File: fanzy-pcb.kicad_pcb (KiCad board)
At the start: 2 copper layers, 68 x 45 mm, 20 parts, among them J1 Conn_01x04_Pin, J2 Screw_Terminal_01x05, Q1 IRLZ44N, SW1 SW_Push, U1 STM32G030F6Px, U4 YAAJ_DCDC_StepDown_LM2596

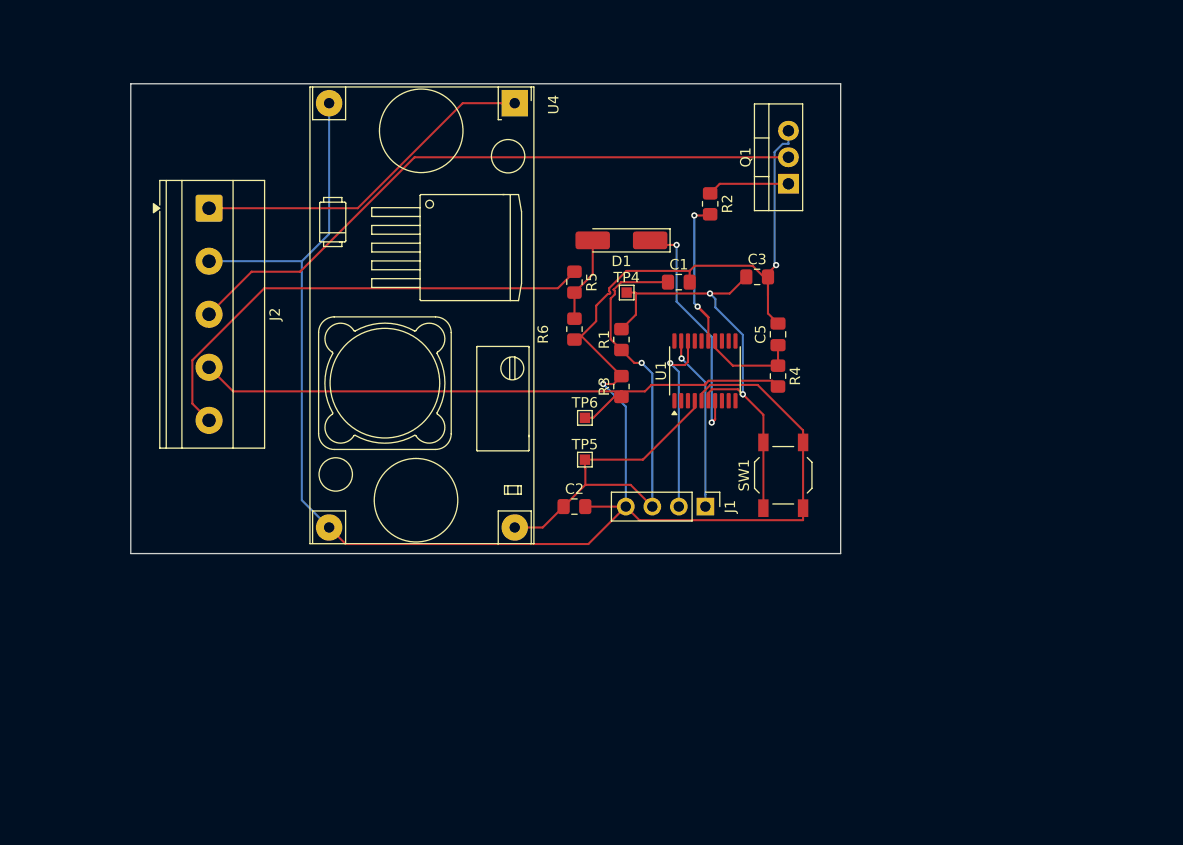
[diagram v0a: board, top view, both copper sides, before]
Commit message: feat: uart port + rework
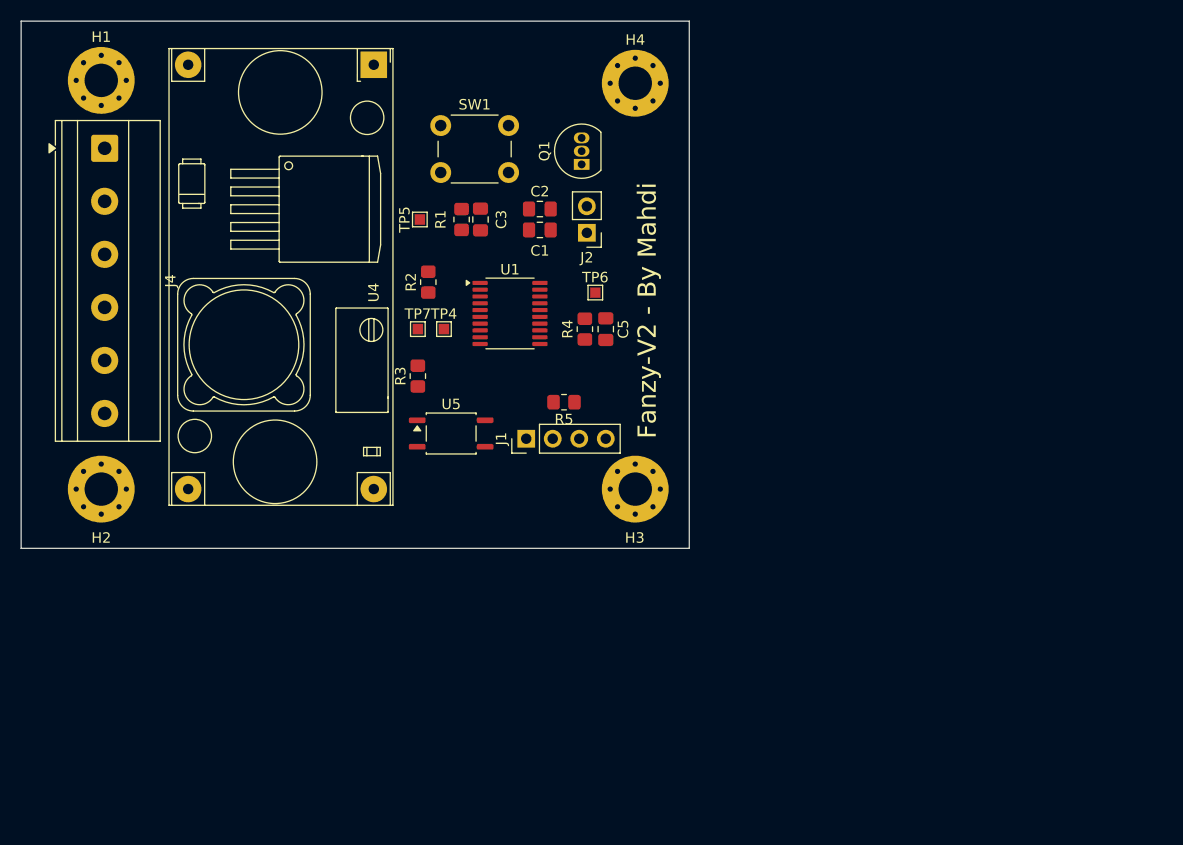
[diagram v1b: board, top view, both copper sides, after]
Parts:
- removed D1: 2V, Diode_SMD:D_MiniMELF_Handsoldering
- removed R6: 10k, Resistor_SMD:R_0805_2012Metric_Pad1.20x1.40mm_HandSolder
- added H1: MountingHole_Pad, MountingHole:MountingHole_3.2mm_M3_Pad_Via, F.Cu at (89.7, 51.2)
- added H2: MountingHole_Pad, MountingHole:MountingHole_3.2mm_M3_Pad_Via, F.Cu at (89.7, 90.3)
- added H3: MountingHole_Pad, MountingHole:MountingHole_3.2mm_M3_Pad_Via, F.Cu at (140.8, 90.3)
- added H4: MountingHole_Pad, MountingHole:MountingHole_3.2mm_M3_Pad_Via, F.Cu at (140.8, 51.5)
- added J4: Screw_Terminal_01x06, TerminalBlock_Phoenix:TerminalBlock_Phoenix_MKDS-1,5-6-5.08_1x06_P5.08mm_Horizontal, F.Cu at (90.0, 57.7)
- added TP7: TestPoint, TestPoint:TestPoint_Pad_1.0x1.0mm, F.Cu at (120.0, 75.0)
- added U5: TLP185, Octocoupler:TLP185, F.Cu at (123.2, 85.0)
- J2: value Screw_Terminal_01x05 -> Conn_01x02_Pin; footprint TerminalBlock_Phoenix:TerminalBlock_Phoenix_MKDS-1,5-5-5.08_1x05_P5.08mm_Horizontal -> Connector_PinHeader_2.54mm:PinHeader_1x02_P2.54mm_Vertical
- Q1: value IRLZ44N -> PN2222A; footprint Package_TO_SOT_THT:TO-220-3_Vertical -> Package_TO_SOT_THT:TO-92_Inline
- R5: value 22k -> 10k
- SW1: footprint Button_Switch_SMD:SW_SPST_TL3342 -> Button_Switch_THT:SW_PUSH_6mm
- U4: footprint YAAJ:YAAJ_DCDC_StepDown_LM2596 -> DC-DC-Converters:YAAJ_DCDC_StepDown_LM2596
- moved SW1 46.9 mm to (122.2, 55.5), turned to 0 degrees
- moved J2 36.3 mm to (136.2, 65.8), turned to 180 degrees
- moved C2 28.7 mm to (131.7, 63.5)
- moved R2 28.0 mm to (121.0, 70.5), turned to 90 degrees
- moved TP5 27.9 mm to (120.2, 64.5), turned to 90 degrees
- moved C3 27.1 mm to (126.0, 64.5), turned to 90 degrees
- moved Q1 19.9 mm to (135.7, 59.2)
- moved R3 19.5 mm to (120.0, 79.5)
- moved U1 19.5 mm to (128.8, 73.5), turned to 0 degrees
- moved R1 19.1 mm to (124.2, 64.5), turned to -90 degrees
- moved R4 19.0 mm to (136.0, 75.0), turned to 90 degrees
- moved J1 18.3 mm to (130.4, 85.5), turned to 90 degrees
- moved TP4 17.8 mm to (122.5, 75.0)
- moved C5 16.5 mm to (138.0, 75.0), turned to -90 degrees
- moved C1 14.2 mm to (131.7, 65.5)
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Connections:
- C1 pad 2: GND -> GNDD
- C2 pad 2: GND -> GNDD
- C3 pad 2: GND -> GNDD
- C5 pad 2: GND -> GNDD
- J1 pad 4: GND -> GNDD
- J2 pad 1: +12V -> /USART2_RX
- J2 pad 2: GND -> /USART2_TX
- Q1 pad 1: Net-(Q1-G) -> GND
- Q1 pad 2: /SIG -> Net-(Q1-B)
- Q1 pad 3: GND -> /SIG
- R2 pad 1: Net-(Q1-G) -> Net-(Q1-B)
- R3 pad 1: /SENS -> Net-(R3-Pad1)
- R3 pad 2: GND -> /AC
- R4 pad 1: /ADC1_IN7 -> GNDD
- R4 pad 2: /SENS -> /ADC1_IN7
- R5 pad 1: /AC -> +3V3
- R5 pad 2: Net-(D1-A) -> /PA0
- SW1 pad 2: GND -> GNDD
- TP6 pad 1: /SENS -> /ADC1_IN7
- U1 pad 10: unconnected-(U1-PA3-Pad10) -> /USART2_RX
- U1 pad 5: GND -> GNDD
- U1 pad 9: unconnected-(U1-PA2-Pad9) -> /USART2_TX
- U4 pad 3: GND -> GNDD
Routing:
- net GND: track 191.0 -> 0.00 mm, vias 2 -> 0
- net /SIG: track 61.7 -> 0.00 mm
- net /SENS: track 61.2 -> 0.00 mm
- net +3V3: track 60.0 -> 0.00 mm, vias 1 -> 0
- net /AC: track 46.5 -> 0.00 mm
- net /NRST: track 44.1 -> 0.00 mm, vias 2 -> 0
- net +12V: track 33.4 -> 0.00 mm
- net /PA0: track 24.3 -> 0.00 mm, vias 2 -> 0
- net /SYS_SWDIO: track 18.0 -> 0.00 mm, vias 1 -> 0
- net /TIM1_CH1 (PA8): track 17.0 -> 0.00 mm, vias 2 -> 0
- net /SYS_SWCLK: track 16.8 -> 0.00 mm, vias 1 -> 0
- net /ADC1_IN7: track 9.36 -> 0.00 mm
- net Net-(D1-A): track 8.22 -> 0.00 mm
- net Net-(Q1-G): track 7.88 -> 0.00 mm
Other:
- board size 68 x 45 mm -> 64 x 50.5 mm
- board text added: "Fanzy-V2 - By Mahdi"

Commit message: rework: switching to the STM32G031J6M6 series
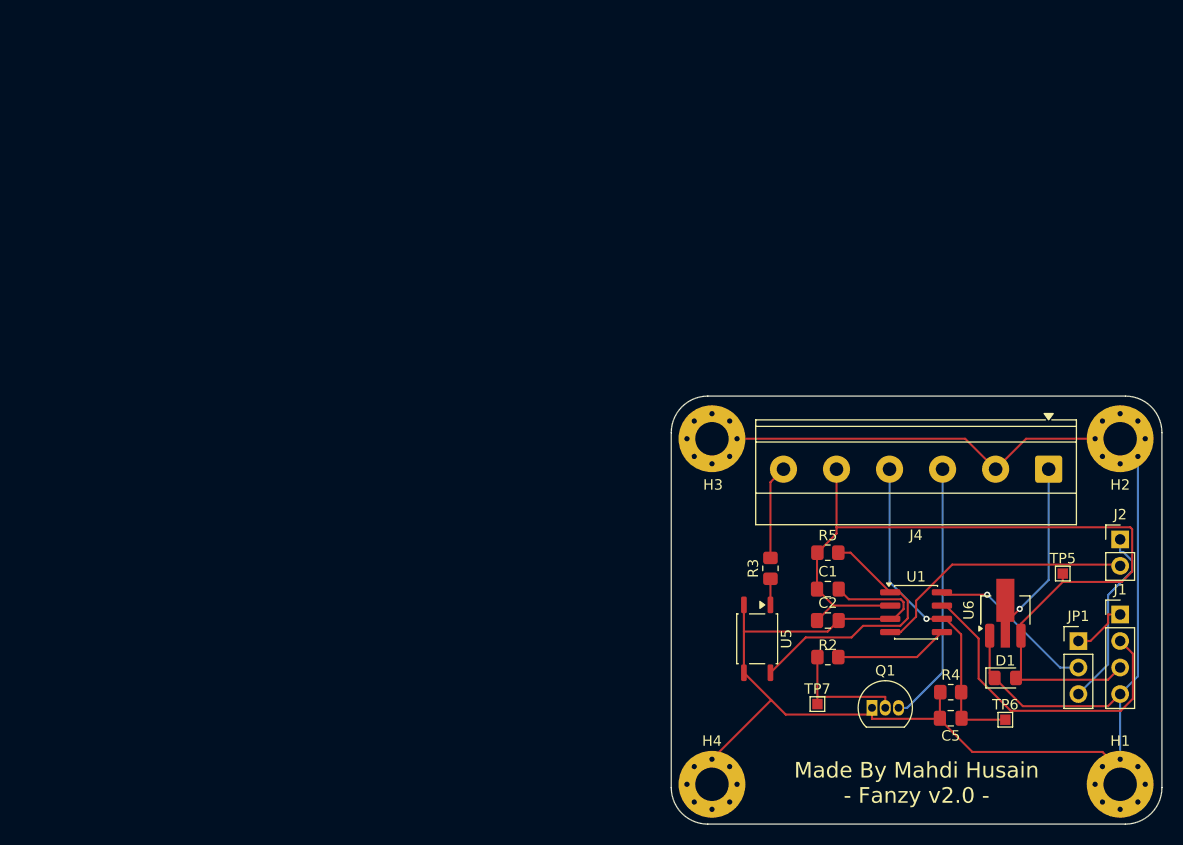
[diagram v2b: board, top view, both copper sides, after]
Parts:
- removed C3: 100nF, Capacitor_SMD:C_0805_2012Metric_Pad1.18x1.45mm_HandSolder
- removed R1: 10k, Resistor_SMD:R_0805_2012Metric_Pad1.20x1.40mm_HandSolder
- removed SW1: SW_Push, Button_Switch_THT:SW_PUSH_6mm
- removed TP4: TestPoint, TestPoint:TestPoint_Pad_1.0x1.0mm
- removed U4: YAAJ_DCDC_StepDown_LM2596, DC-DC-Converters:YAAJ_DCDC_StepDown_LM2596
- added D1: LED, LED_SMD:LED_0805_2012Metric_Pad1.15x1.40mm_HandSolder, F.Cu at (176.3, 108.4)
- added JP1: Jumper_3_Bridged12, Connector_PinHeader_2.54mm:PinHeader_1x03_P2.54mm_Vertical, F.Cu at (183.3, 104.9)
- added U6: HT75xx-1-SOT89, Package_TO_SOT_SMD:SOT-89-3_Handsoldering, F.Cu at (176.3, 101.9)
- U1: value STM32G030F6Px -> STM32G031J6Mx; footprint Package_SO:TSSOP-20_4.4x6.5mm_P0.65mm -> Package_SO:SOIC-8_3.9x4.9mm_P1.27mm
- moved H1 118.6 mm to (187.3, 118.6)
- moved H2 97.7 mm to (187.3, 85.5)
- moved J4 95.5 mm to (180.4, 88.4), turned to 180 degrees
- moved TP5 70.3 mm to (181.8, 98.4), turned to 0 degrees
- moved H4 67.6 mm to (148.2, 118.6)
- moved J1 59.3 mm to (187.3, 102.3), turned to 0 degrees
- moved Q1 59.0 mm to (163.5, 111.3), turned to 0 degrees
- moved J2 58.9 mm to (187.3, 95.1), turned to 0 degrees
- moved TP6 56.7 mm to (176.3, 112.4)
- moved R2 52.5 mm to (159.3, 106.4), turned to 0 degrees
- moved TP7 52.5 mm to (158.3, 110.9)
- moved C5 49.8 mm to (171.0, 112.3), turned to 180 degrees
- moved R4 49.4 mm to (171.0, 109.8), turned to 0 degrees
- moved U1 48.3 mm to (167.7, 102.1)
- moved C2 48.1 mm to (159.3, 102.9)
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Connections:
- C1 pad 2: GNDD -> GND
- C2 pad 2: GNDD -> GND
- C5 pad 1: /ADC1_IN7 -> /ADC1_IN1 (PA1)
- C5 pad 2: GNDD -> GND
- J1 pad 4: GNDD -> GND
- J2 pad 1: /USART2_RX -> /USART2_RX (PA15)
- J2 pad 2: /USART2_TX -> /USART2_TX (PA2)
- J4 pad 4: /ADC1_IN7 -> /ADC1_IN1 (PA1)
- R4 pad 1: GNDD -> GND
- R4 pad 2: /ADC1_IN7 -> /ADC1_IN1 (PA1)
- R5 pad 2: /PA0 -> /PB7/PB8/PB9/PC14
- TP6 pad 1: /ADC1_IN7 -> /ADC1_IN1 (PA1)
- U1 pad 1: unconnected-(U1-PB7/PB8-Pad1) -> /PB7/PB8/PB9/PC14
- U1 pad 2: unconnected-(U1-PB9/PC14-Pad2) -> +3V3
- U1 pad 3: unconnected-(U1-PC15-Pad3) -> GND
- U1 pad 4: +3V3 -> /USART2_TX (PA2)
- U1 pad 5: GNDD -> /TIM1_CH1 (PA8)
- U1 pad 6: /NRST -> /ADC1_IN1 (PA1)
- U1 pad 7: /PA0 -> /SYS_SWDIO
- U1 pad 8: unconnected-(U1-PA1-Pad8) -> Net-(JP1-C)
- U5 pad 4: GNDD -> GND
- U5 pad 6: /PA0 -> /PB7/PB8/PB9/PC14
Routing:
- net GND: track 0.00 -> 228.7 mm
- net +3V3: track 0.00 -> 84.0 mm
- net /ADC1_IN1 (PA1): track 0.00 -> 32.0 mm, vias 0 -> 1
- net /SYS_SWDIO: track 0.00 -> 31.2 mm
- net /USART2_TX (PA2): track 0.00 -> 25.6 mm
- net /PB7/PB8/PB9/PC14: track 0.00 -> 25.6 mm
- net /SIG: track 0.00 -> 25.1 mm
- net +12V: track 0.00 -> 17.6 mm, vias 0 -> 1
- net /USART2_RX (PA15): track 0.00 -> 17.6 mm
- net Net-(JP1-C): track 0.00 -> 16.1 mm, vias 0 -> 1
- net Net-(Q1-B): track 0.00 -> 12.1 mm
- net /TIM1_CH1 (PA8): track 0.00 -> 10.9 mm
- net /AC: track 0.00 -> 9.02 mm
- net /SYS_SWCLK: track 0.00 -> 5.55 mm
- net Net-(R3-Pad1): track 0.00 -> 2.50 mm
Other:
- board size 64 x 50.5 mm -> 47 x 41 mm
- board text added: "Made By Mahdi Husain - Fanzy v2.0 -"
- board text removed: "Fanzy-V2 - By Mahdi"
